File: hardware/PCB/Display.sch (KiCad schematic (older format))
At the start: 9 parts

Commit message: edited display circuit
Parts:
- added C? (x2): 4u7, Capacitor_SMD:C_0603_1608Metric, symbol Device:C
- added D? (x3): MBR0530, Diode_SMD:D_SOD-123, symbol Diode:MBR0530
- added L?: 68u, Inductor_SMD:L_0805_2012Metric, symbol pspice:INDUCTOR
- added Q?: SI1308EDL-T1-BE3, SOT65P210X110-3N, symbol ProjectLibrary:SI1308EDL-T1-BE3
- added R?: 10k, Resistor_SMD:R_0603_1608Metric, symbol Device:R
- added R?: 3R0, Resistor_SMD:R_0603_1608Metric, symbol Device:R
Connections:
- net +3V3: now also C?.1, L?.2
- net GND: now also C?.2, D?.1 (K), R?.1, R?.2
- net PREVGH: now also D?.1 (K)
- net PREVGL: now also D?.2 (A)
- net GDR: now reaches J?.2
- net GDR: now also Q?.1, R?.1
- net RESE: now reaches J?.3
- net RESE: now also Q?.2, R?.2
- new net: C?.2, D?.1 (K), D?.2 (A)
- new net: C?.1, D?.2 (A), L?.1, Q?.3
- no-connect marks 0 -> 3
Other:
- moved on the sheet: C?, J?

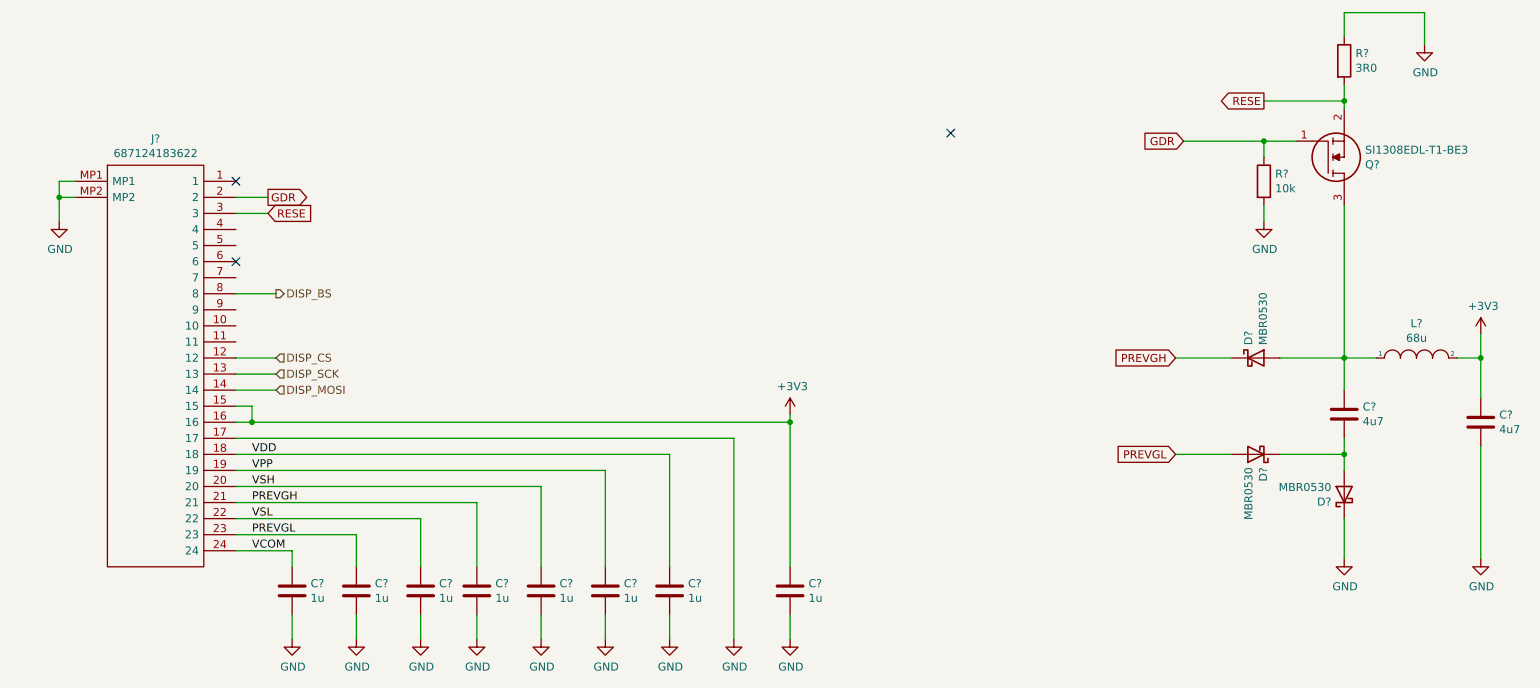
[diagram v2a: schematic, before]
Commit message: complete display circuit
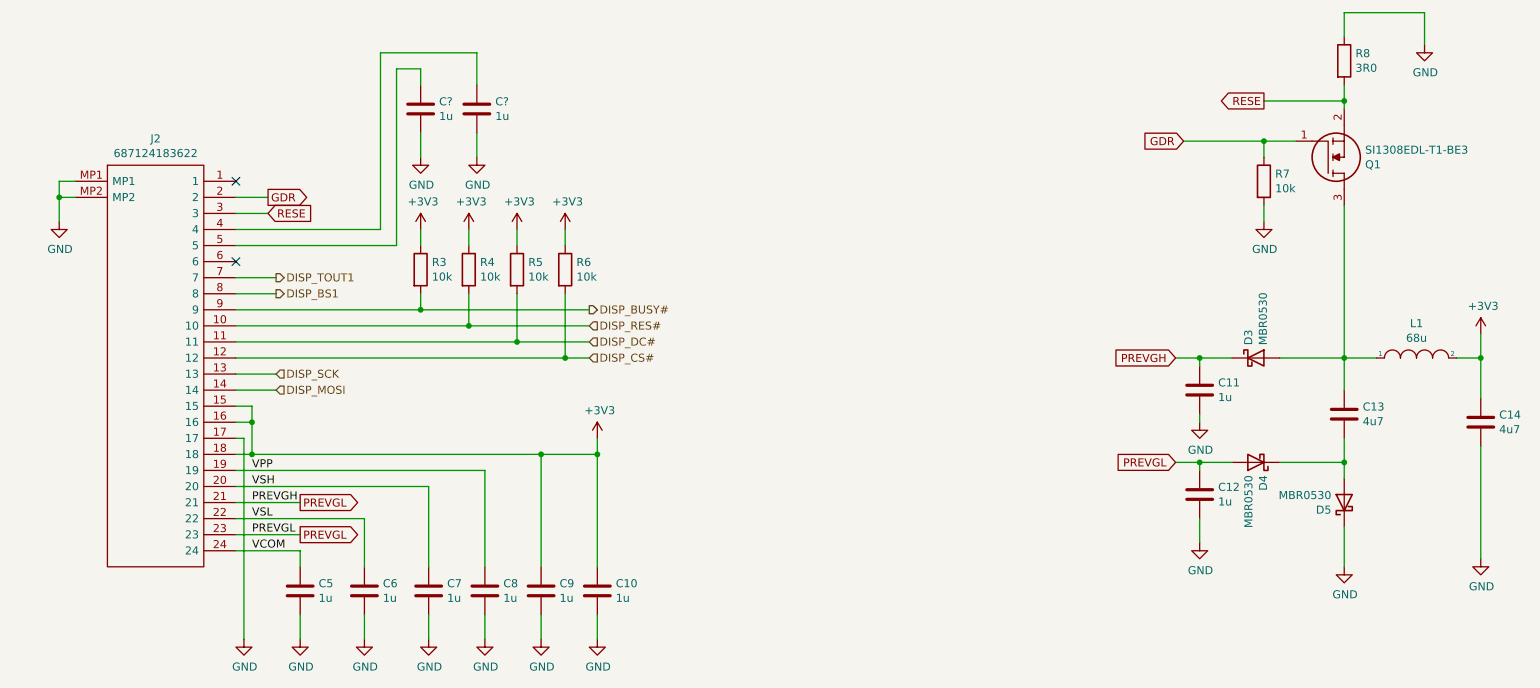
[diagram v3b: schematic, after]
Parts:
- removed C? (x2): 1u, Capacitor_SMD:C_0603_1608Metric, symbol Device:C
- added C11, C12, C? (x2): 1u, Capacitor_SMD:C_0603_1608Metric, symbol Device:C
- added R3, R4, R5, R6: 10k, Resistor_SMD:R_0603_1608Metric, symbol Device:R
- gave numbers to parts that had none: 16
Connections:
- net PREVGL is gone; now on net PREVGH: D4.2 (A), J2.23
- net VDD is gone; now on net +3V3: C9.1, J2.18
- net +3V3: now also R3.1, R4.1, R5.1, R6.1
- net GND: now also C11.2, C12.2, C?.2, C?.2
- net PREVGH: now also C11.1, C12.1
- net DISP_RES#: now reaches J2.10
- net DISP_RES#: now also R4.2
- net DISP_DC#: now reaches J2.11
- net DISP_DC#: now also R5.2
- net at J2.4: now also C?.1
- net at J2.5: now also C?.1
- net DISP_TOUT1: now reaches J2.7
- net DISP_BUSY#: now reaches J2.9
- net DISP_BUSY#: now also R3.2
- net DISP_BS renamed DISP_BS1
- net DISP_CS renamed DISP_CS#
- net DISP_CS#: now also R6.2
- no-connect marks 3 -> 2
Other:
- moved on the sheet: C10, C5, C6, C7, C8, C9, D4, D5

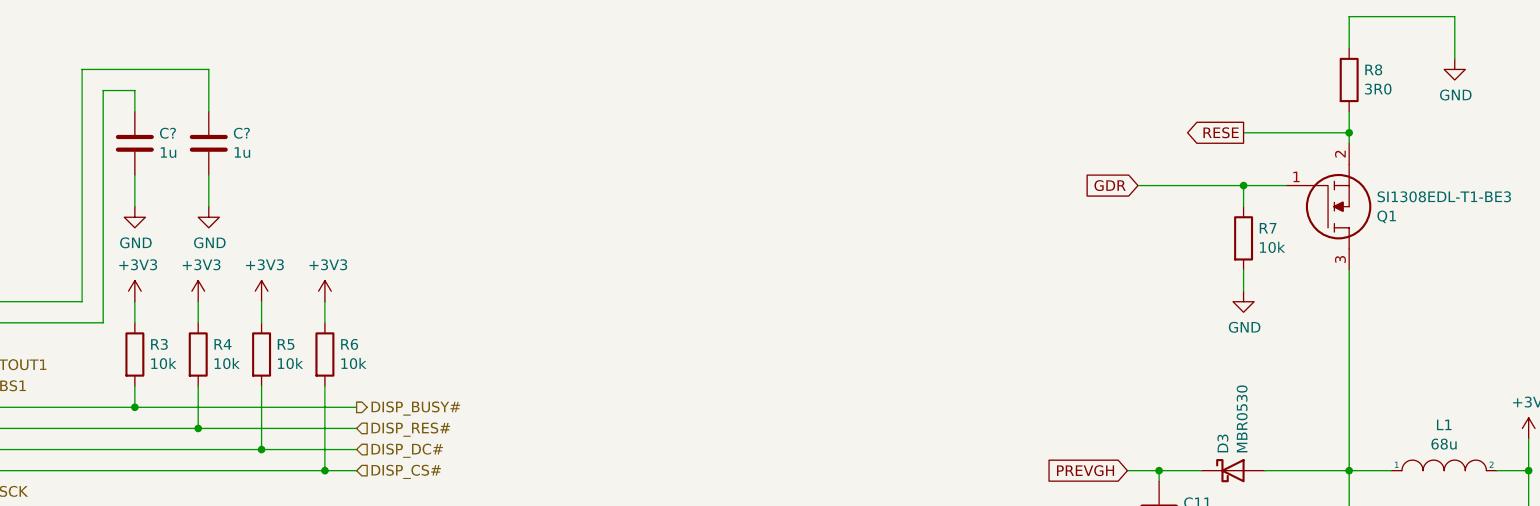
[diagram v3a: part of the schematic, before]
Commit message: add ESP32 and Sensor Sheet
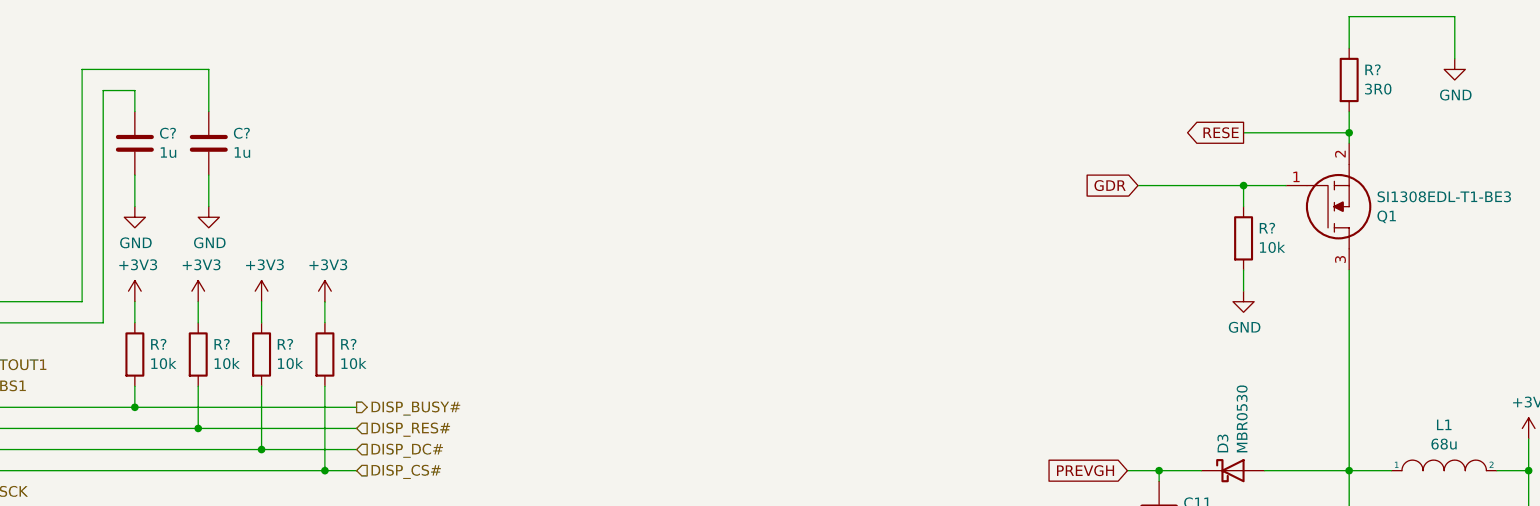
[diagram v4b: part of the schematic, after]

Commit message: add 10k pull up
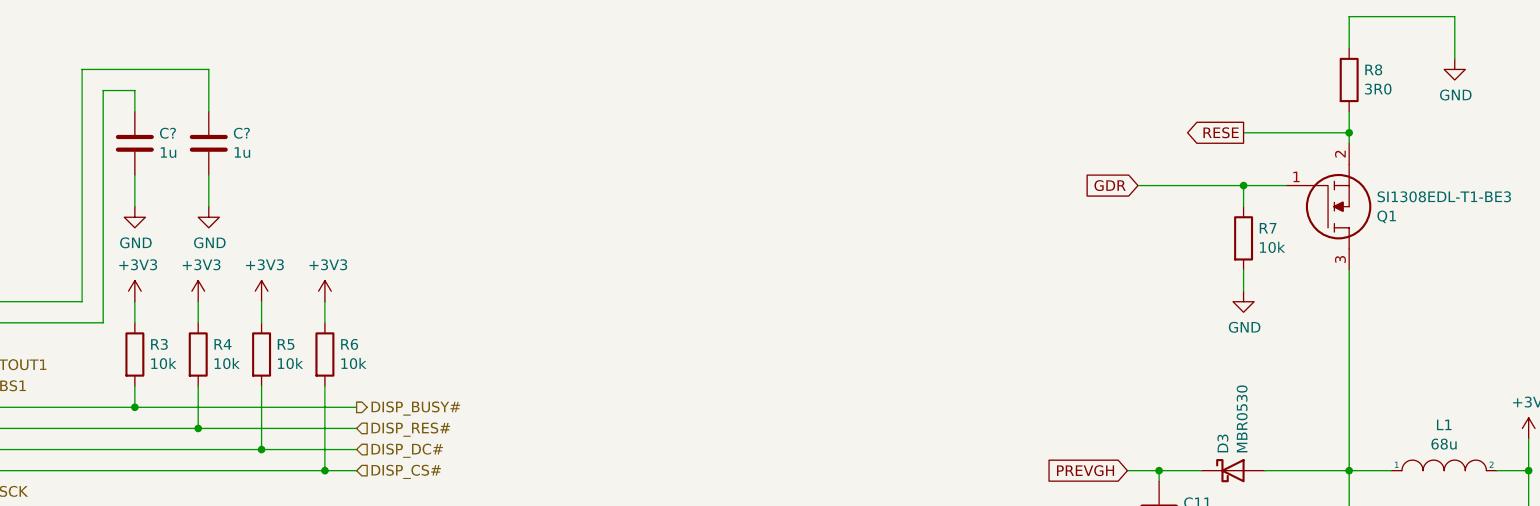
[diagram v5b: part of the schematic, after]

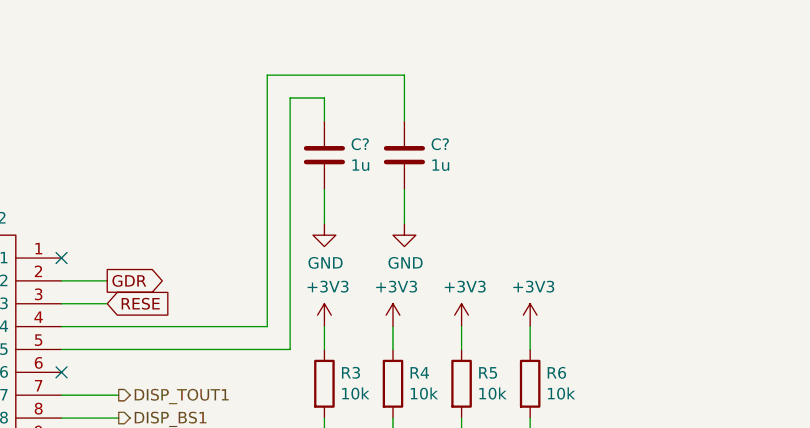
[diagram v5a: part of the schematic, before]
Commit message: add mechannical and usb ftdi sheet
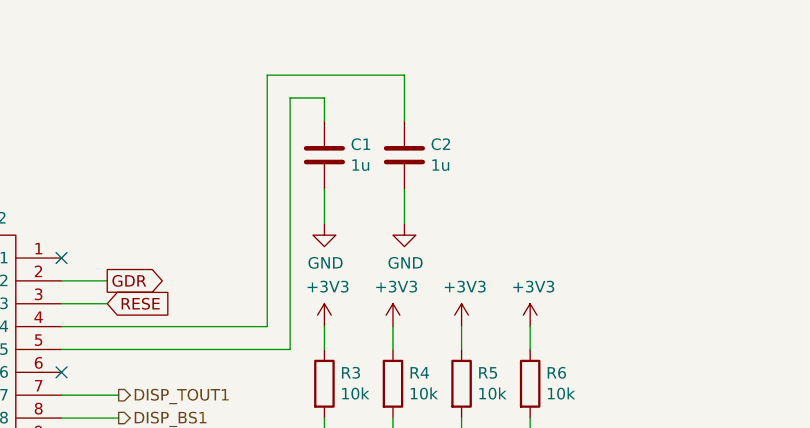
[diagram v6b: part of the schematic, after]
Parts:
- gave numbers to parts that had none: 2
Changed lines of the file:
@@
 $Descr A4 11693 8268
 encoding utf-8
-Sheet 3 5
+Sheet 3 7
 Title ""
 Date ""
@@
 	2300 4900 2700 4900
 $Comp
-L Device:C C?
+L Device:C C1
 U 1 1 5FCC1A18
 P 3450 2150
-AR Path="/5FC321F3/5FCC1A18" Ref="C?"  Part="1"
+AR Path="/5FC321F3/5FCC1A18" Ref="C1"  Part="1"
 AR Path="/5FCF3C77/5FCC1A18" Ref="C?"  Part="1"
-F 0 "C?" H 3565 2196 50  0000 L CNN
+F 0 "C1" H 3565 2196 50  0000 L CNN
 F 1 "1u" H 3565 2105 50  0000 L CNN
 F 2 "Capacitor_SMD:C_0603_1608Metric" H 3488 2000 50  0001 C CNN
@@
 	3450 2300 3450 2450
 $Comp
-L power:GND #PWR?
+L power:GND #PWR034
 U 1 1 5FCC1A1F
 P 3450 2450
-AR Path="/5FC321F3/5FCC1A1F" Ref="#PWR?"  Part="1"
+AR Path="/5FC321F3/5FCC1A1F" Ref="#PWR034"  Part="1"
 AR Path="/5FCF3C77/5FCC1A1F" Ref="#PWR?"  Part="1"
-F 0 "#PWR?" H 3450 2200 50  0001 C CNN
+F 0 "#PWR034" H 3450 2200 50  0001 C CNN
 F 1 "GND" H 3455 2277 50  0000 C CNN
 F 2 "" H 3450 2450 50  0001 C CNN
@@
 $EndComp
 $Comp
-L Device:C C?
+L Device:C C2
 U 1 1 5FCC1A25
 P 3800 2150
-AR Path="/5FC321F3/5FCC1A25" Ref="C?"  Part="1"
+AR Path="/5FC321F3/5FCC1A25" Ref="C2"  Part="1"
 AR Path="/5FCF3C77/5FCC1A25" Ref="C?"  Part="1"
-F 0 "C?" H 3915 2196 50  0000 L CNN
+F 0 "C2" H 3915 2196 50  0000 L CNN
 F 1 "1u" H 3915 2105 50  0000 L CNN
 F 2 "Capacitor_SMD:C_0603_1608Metric" H 3838 2000 50  0001 C CNN
@@
 $EndComp
 $Comp
-L power:GND #PWR?
+L power:GND #PWR035
 U 1 1 5FCC1A2B
 P 3800 2450
-AR Path="/5FC321F3/5FCC1A2B" Ref="#PWR?"  Part="1"
+AR Path="/5FC321F3/5FCC1A2B" Ref="#PWR035"  Part="1"
 AR Path="/5FCF3C77/5FCC1A2B" Ref="#PWR?"  Part="1"
-F 0 "#PWR?" H 3800 2200 50  0001 C CNN
+F 0 "#PWR035" H 3800 2200 50  0001 C CNN
 F 1 "GND" H 3805 2277 50  0000 C CNN
 F 2 "" H 3800 2450 50  0001 C CNN

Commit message: component placement done
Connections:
- net PREVGH: no longer C12.1, D4.2 (A), J2.23
- new net PREVGL: C12.1, D4.2 (A), J2.23
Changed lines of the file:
@@
 	2300 4800 2700 4800
 Text GLabel 2700 4600 2    50   Output ~ 0
-PREVGL
+PREVGH
 Wire Wire Line
 	2300 4600 2700 4600
